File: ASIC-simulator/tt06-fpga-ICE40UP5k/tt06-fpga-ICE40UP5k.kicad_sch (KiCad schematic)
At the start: 14 parts, among them CON1 NPTC202KFMS-RC, CON2 NPTC202KFMS-RC

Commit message: LCSC components and minor layout tweaks for production run
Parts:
- R1: LCSC (none) -> C106235
- TP3, TP4, TP5, TP6, TP7: LCSC (none) -> C5199800; MPN (none) -> 5019

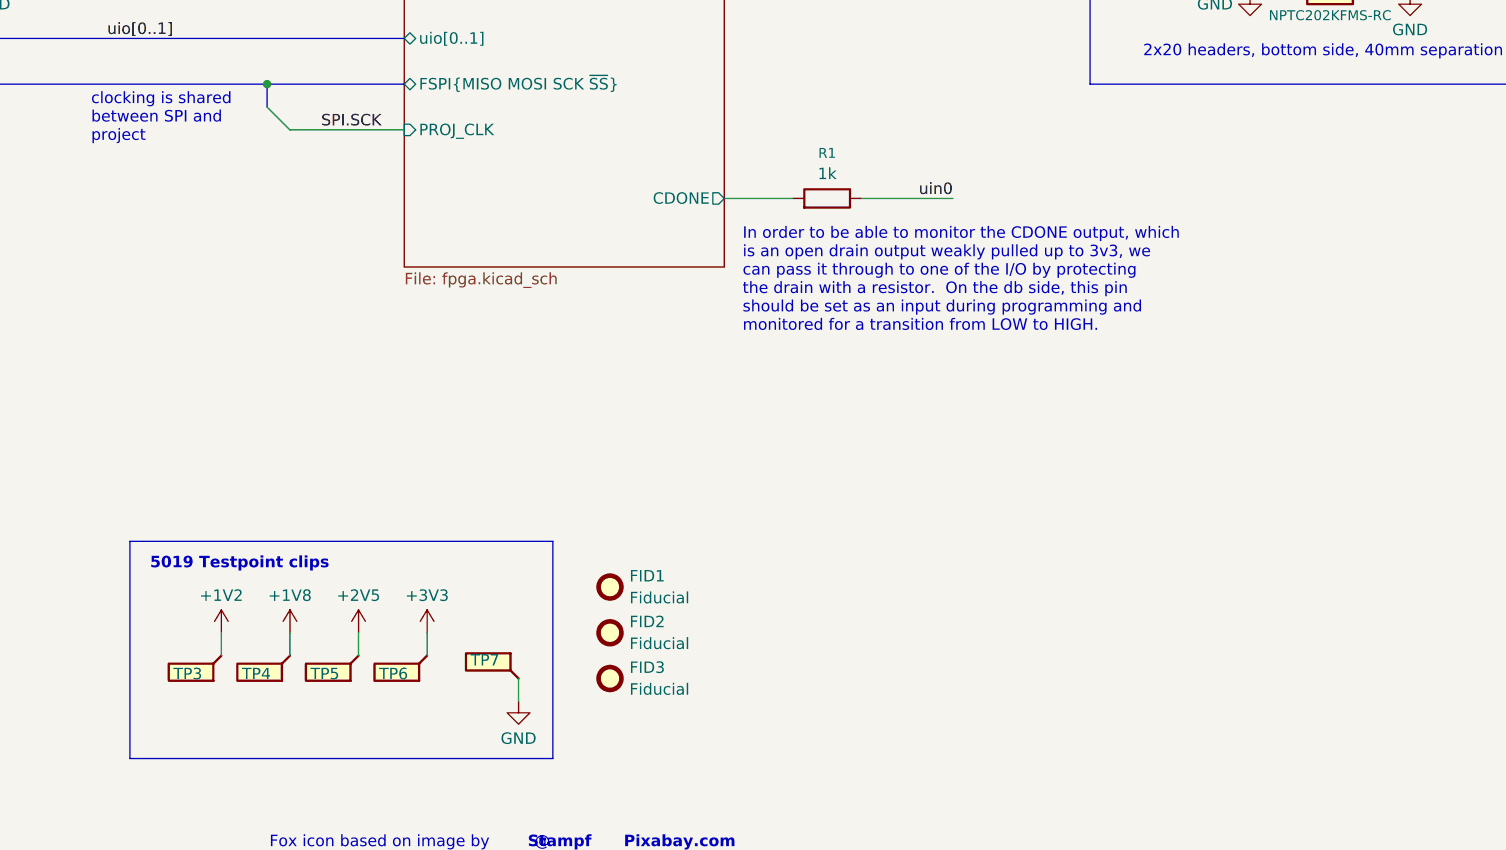
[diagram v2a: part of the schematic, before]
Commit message: v1.1 CDONE LED
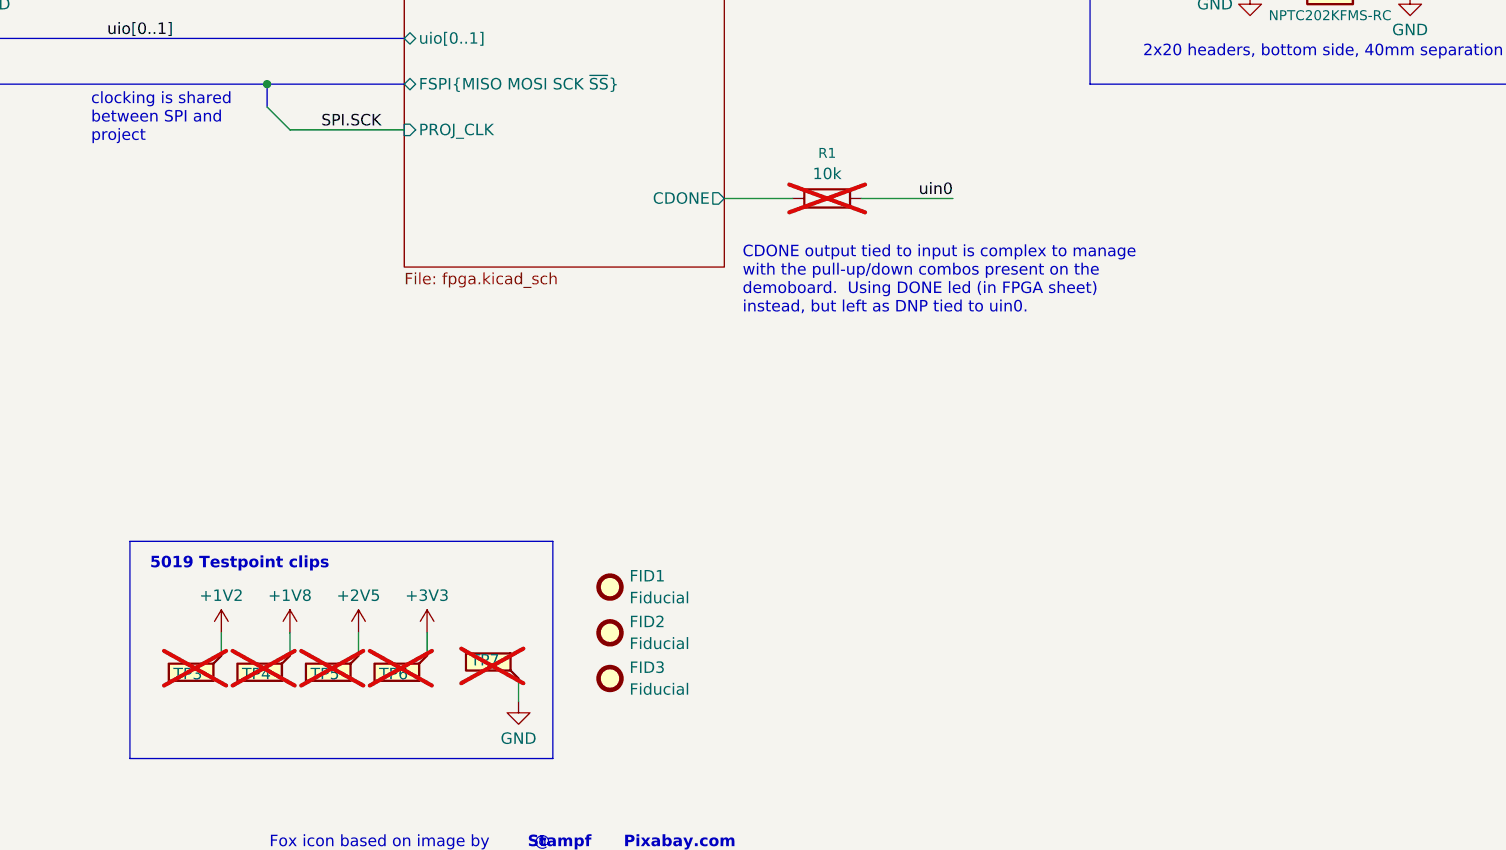
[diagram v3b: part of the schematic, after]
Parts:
- removed R1: 1k, Resistor_SMD:R_0402_1005Metric, symbol psycomponents:PsyResistors_IEC/R_1k_0402_1005-18
- added R1: 10k, Resistor_SMD:R_0402_1005Metric, symbol psycomponents:PsyResistors_IEC/R_10k_0402_1005-12
- TP3, TP4, TP5, TP6, TP7: now not fitted
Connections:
- net FPGA/CDONE: now also R1.1
- net uin0: now also R1.2
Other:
- note added: "CDONE output tied to input is complex to manage with the pull-up/down combos present on the demoboard. Using DONE led (in FPGA sheet) instead, but left as DNP tied to uin0."
- note removed: "In order to be able to monitor the CDONE output, which is an open drain output weakly pulled up to 3v3, we can pass it through to one of the I/O by protecting the drain with a resistor. On the db side, this pin should be set as an input during programming and monitored for a transition from LOW to HIGH."
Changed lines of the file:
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@@
 	(title_block
 		(title "FabricFox FPGASIC")
-		(date "2025-06-24")
-		(rev "1.0")
+		(date "2025-08-01")
+		(rev "1.1")
 		(company "Psychogenic Technologies INC")
 		(comment 1 "(C) 2025 Pat Deegan")
@@
 		)
 	)
-	(text "In order to be able to monitor the CDONE output, which \nis an open drain output weakly pulled up to 3v3, we \ncan pass it through to one of the I/O by protecting \nthe drain with a resistor.  On the db side, this pin \nshould be set as an input during programming and \nmonitored for a transition from LOW to HIGH."
+	(text "CDONE output tied to input is complex to manage\nwith the pull-up/down combos present on the \ndemoboard.  Using DONE led (in FPGA sheet)\ninstead, but left as DNP tied to uin0."
 		(exclude_from_sim no)
 		(at 174.752 133.604 0)
@@
 		(in_bom yes)
 		(on_board yes)
-		(dnp no)
+		(dnp yes)
 		(property "Reference" "TP7"
 			(at 144.526 175.768 0)
@@
 		(in_bom yes)
 		(on_board yes)
-		(dnp no)
+		(dnp yes)
 		(property "Reference" "TP3"
 			(at 111.506 177.292 0)
@@
 		(in_bom yes)
 		(on_board yes)
-		(dnp no)
+		(dnp yes)
 		(property "Reference" "TP6"
 			(at 134.366 177.292 0)
@@
 		(in_bom yes)
 		(on_board yes)
-		(dnp no)
+		(dnp yes)
 		(property "Reference" "TP4"
 			(at 119.126 177.292 0)
@@
 	)
 	(symbol
+		(lib_id "psycomponents:PsyResistors_IEC/R_10k_0402_1005-12")
+		(at 180.34 124.46 90)
+		(unit 1)
+		(exclude_from_sim no)
+		(in_bom yes)
+		(on_board yes)
+		(dnp yes)
+		(fields_autoplaced yes)
+		(property "Reference" "R1"
+			(at 184.15 119.4363 90)
+			(effects
+				(font
+					(size 1.1 1.1)
+				)
+			)
+		)
+		(property "Value" "10k"
+			(at 184.15 121.7238 90)
+			(effects
+				(font
+					(size 1.27 1.27)
+				)
+			)
+		)
+		(property "Footprint" "Resistor_SMD:R_0402_1005Metric"
+			(at 180.34 126.238 90)
+			(effects
+				(font
+					(size 1.27 1.27)
+				)
+				(hide yes)
+			)
+		)
+		(property "Datasheet" "https://industrial.panasonic.com/cdbs/www-data/pdf/RDP0000/AOA0000C334.pdf"
+			(at 180.34 124.46 0)
+			(effects
+				(font
+					(size 1.27 1.27)
+				)
+				(hide yes)
+			)
+		)
+		(property "Description" "10 kOhms ±1% 0.1W, 1/10W Chip Resistor 0402 (1005 Metric) Anti-Sulfur, Automotive AEC-Q200 Thick Film"
+			(at 184.658 122.428 90)
+			(effects
+				(font
+					(size 1.27 1.27)
+				)
+				(hide yes)
+			)
+		)
+		(property "MPN" "ERJ-U02F1002X"
+			(at 180.34 124.46 0)
+			(show_name yes)
+			(effects
+				(font
+					(size 1.27 1.27)
+				)
+				(hide yes)
+			)
+		)
+		(property "Manufacturer" "Panasonic Electronic Components"
+			(at 180.34 124.46 0)
+			(effects
+				(font
+					(size 1.27 1.27)
+				)
+				(hide yes)
+			)
+		)
+		(property "Package / Case" "0402 (1005 Metric)"
+			(at 180.34 124.46 0)
+			(effects
+				(font
+					(size 1.27 1.27)
+				)
+				(hide yes)
+			)
+		)
+		(property "Characteristics" "RES 10K OHM 1% 1/10W 0402"
+			(at 180.34 124.46 0)
+			(effects
+				(font
+					(size 1.27 1.27)
+				)
+				(hide yes)
+			)
+		)
+		(property "DigikeyPN" "10-ERJ-U02F1002XCT-ND"
+			(at 180.34 124.46 0)
+			(effects
+				(font
+					(size 1.27 1.27)
+				)
+				(hide yes)
+			)
+		)
+		(property "LCSC" "C60490"
+			(at 180.34 124.46 0)
+			(show_name yes)
+			(effects
+				(font
+					(size 1.27 1.27)
+				)
+				(hide yes)
+			)
+		)
+		(property "MPN_ALT" ""
+			(at 180.34 124.46 0)
+			(show_name yes)
+			(effects
+				(font
+					(size 1.27 1.27)
+				)
+				(hide yes)
+			)
+		)
+		(property "Display Value" ""
+			(at 180.34 124.46 0)
+			(effects
+				(font
+					(size 1.27 1.27)
+				)
+				(hide yes)
+			)
+		)
+		(property "Display_Value" ""
+			(at 180.34 124.46 0)
+			(effects
+				(font
+					(size 1.27 1.27)
+				)
+				(hide yes)
+			)
+		)
+		(property "Variant" ""
+			(at 180.34 124.46 0)
+			(effects
+				(font
+					(size 1.27 1.27)
+				)
+				(hide yes)
+			)
+		)
+		(property "Note" ""
+			(at 180.34 124.46 0)
+			(effects
+				(font
+					(size 1.27 1.27)
+				)
+			)
+		)
+		(property "Component Class" ""
+			(at 180.34 124.46 0)
+			(effects
+				(font
+					(size 1.27 1.27)
+				)
+			)
+		)
+		(pin "2"
+		)
+		(pin "1"
+		)
+		(instances
+			(project "tt06-fpga-ICE40UP5k"
+				(path "/5f27e142-b8a6-4247-837b-e9330245c956"
+					(reference "R1")
+					(unit 1)
+				)
+			)
+		)
+	)
+	(symbol
 		(lib_id "power:+1V8")
 		(at 55.88 60.96 0)
@@
 		(in_bom yes)
 		(on_board yes)
-		(dnp no)
+		(dnp yes)
 		(property "Reference" "TP5"
 			(at 126.746 177.292 0)
@@
 					(unit 1)
 				)
-			)
-		)
-	)
-	(symbol
-		(lib_id "psycomponents:PsyResistors_IEC/R_1k_0402_1005-18")
-		(at 180.34 124.46 90)
-		(unit 1)
-		(exclude_from_sim no)
-		(in_bom yes)
-		(on_board yes)
-		(dnp no)
-		(fields_autoplaced yes)
-		(property "Reference" "R1"
-			(at 184.15 119.4363 90)
-			(effects
-				(font
-					(size 1.1 1.1)
-				)
-			)
-		)
-		(property "Value" "1k"
-			(at 184.15 121.7238 90)
-			(effects
-				(font
-					(size 1.27 1.27)
-				)
-			)
-		)
-		(property "Footprint" "Resistor_SMD:R_0402_1005Metric"
-			(at 180.34 126.238 90)
-			(effects
-				(font
-					(size 1.27 1.27)
-				)
-				(hide yes)
-			)
-		)
-		(property "Datasheet" "https://www.te.com/commerce/DocumentDelivery/DDEController?Action=srchrtrv&DocNm=1773204&DocType=DS&DocLang=English"
-			(at 180.34 124.46 0)
-			(effects
-				(font
-					(size 1.27 1.27)
-				)
-				(hide yes)
-			)
-		)
-		(property "Description" "1 kOhms ±1% 0.063W, 1/16W Chip Resistor 0402 (1005 Metric) Thick Film"
-			(at 184.658 122.428 90)
-			(effects
-				(font
-					(size 1.27 1.27)
-				)
-				(hide yes)
-			)
-		)
-		(property "MPN" "CRG0402F1K0"
-			(at 180.34 124.46 0)
-			(show_name yes)
-			(effects
-				(font
-					(size 1.27 1.27)
-				)
-				(hide yes)
-			)
-		)
-		(property "Manufacturer" "TE Connectivity Passive Product"
-			(at 180.34 124.46 0)
-			(effects
-				(font
-					(size 1.27 1.27)
-				)
-				(hide yes)
-			)
-		)
-		(property "Package / Case" "0402 (1005 Metric)"
-			(at 180.34 124.46 0)
-			(effects
-				(font
-					(size 1.27 1.27)
-				)
-				(hide yes)
-			)
-		)
-		(property "Characteristics" "RES SMD 1K OHM 1% 1/16W 0402"
-			(at 180.34 124.46 0)
-			(effects
-				(font
-					(size 1.27 1.27)
-				)
-				(hide yes)
-			)
-		)
-		(property "DigikeyPN" "A121534CT-ND"
-			(at 180.34 124.46 0)
-			(effects
-				(font
-					(size 1.27 1.27)
-				)
-				(hide yes)
-			)
-		)
-		(property "LCSC" "C106235"
-			(at 180.34 124.46 0)
-			(show_name yes)
-			(effects
-				(font
-					(size 1.27 1.27)
-				)
-				(hide yes)
-			)
-		)
-		(property "MPN_ALT" ""
-			(at 180.34 124.46 0)
-			(show_name yes)
-			(effects
-				(font
-					(size 1.27 1.27)
-				)
-				(hide yes)
-			)
-		)
-		(property "Display Value" ""
-			(at 180.34 124.46 90)
-			(effects
-				(font
-					(size 1.27 1.27)
-				)
-				(hide yes)
-			)
-		)
-		(property "Display_Value" ""
-			(at 180.34 124.46 90)
-			(effects
-				(font
-					(size 1.27 1.27)
-				)
-				(hide yes)
-			)
-		)
-		(pin "2"
-		)
-		(pin "1"
-		)
-		(instances
-			(project ""
-				(path "/5f27e142-b8a6-4247-837b-e9330245c956"
-					(reference "R1")
-					(unit 1)
-				)
